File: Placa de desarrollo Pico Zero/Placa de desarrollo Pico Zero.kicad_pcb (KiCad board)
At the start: 2 copper layers, 91.5 x 101.6 mm, 33 parts, among them J1 LEFT-MALE, J2 RIGHT-MALE, J3 DOWN-MALE, J4 DOWN-FEMALE, J5 LEFT-FEMALE, J6 RIGHT-FEMALE, J7 USB_A, U1 RP2040

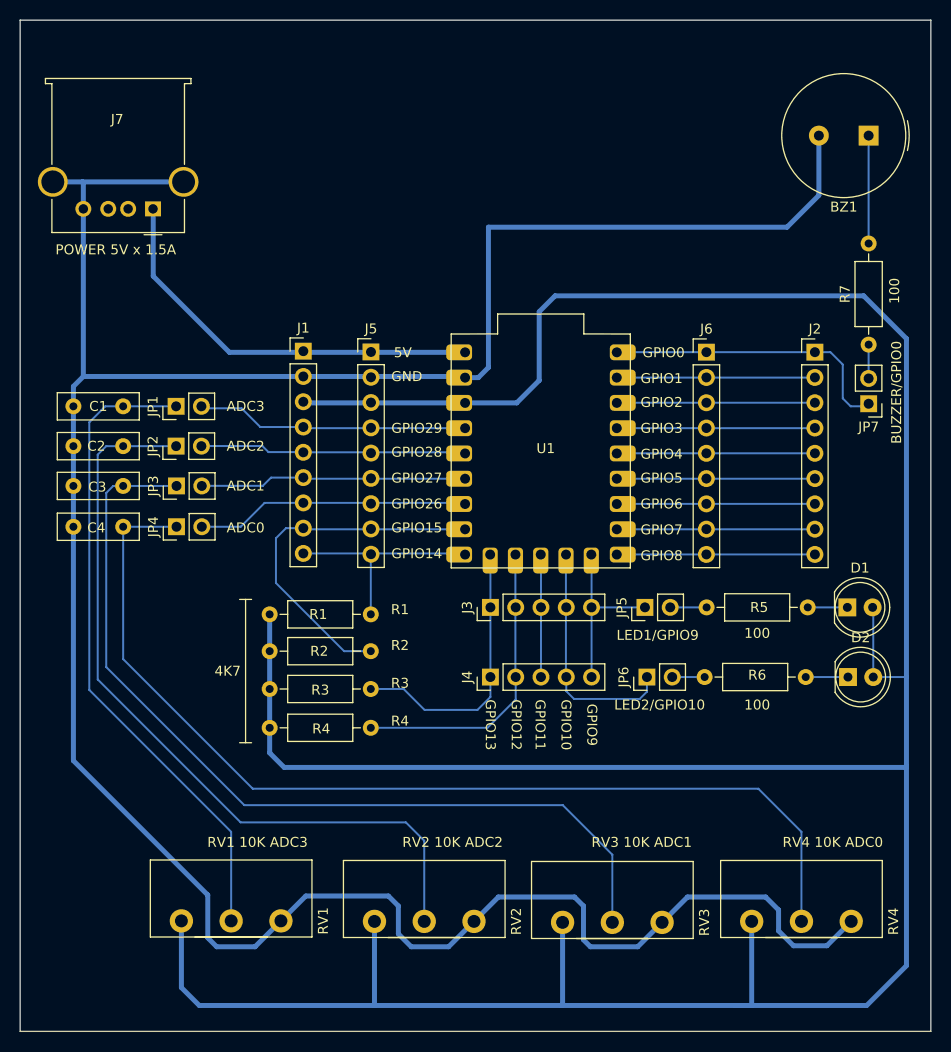
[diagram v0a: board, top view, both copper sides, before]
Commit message: Version 1.0 de la placa de desarrollor para la Pico Zero
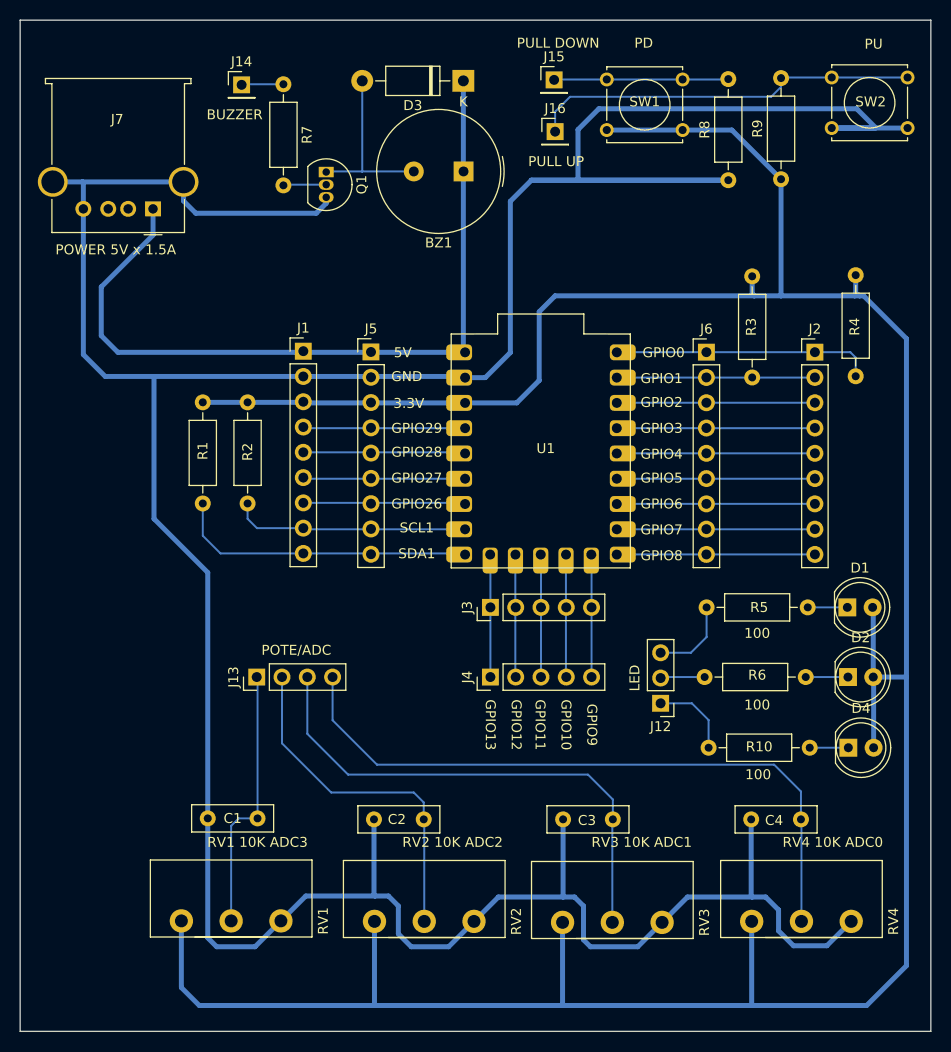
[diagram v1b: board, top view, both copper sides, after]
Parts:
- removed JP1, JP2, JP3, JP4, JP5, JP6, JP7: Jumper_2_Bridged, Connector_PinHeader_2.54mm:PinHeader_1x02_P2.54mm_Vertical
- added D3: 1N4007, Diode_THT:D_DO-41_SOD81_P10.16mm_Horizontal, F.Cu at (142.1, 22.7)
- added D4: LED, LED_THT:LED_D5.0mm, F.Cu at (180.8, 89.7)
- added J12: Conn_01x03, Connector_PinHeader_2.54mm:PinHeader_1x03_P2.54mm_Vertical, F.Cu at (161.9, 85.2)
- added J13: Conn_01x04, Connector_PinHeader_2.54mm:PinHeader_1x04_P2.54mm_Vertical, F.Cu at (121.3, 82.6)
- added J14: Conn_01x01, Connector_PinHeader_2.54mm:PinHeader_1x01_P2.54mm_Vertical, F.Cu at (119.8, 23.1)
- added J15: Conn_01x01, Connector_PinHeader_2.54mm:PinHeader_1x01_P2.54mm_Vertical, F.Cu at (151.2, 22.6)
- added J16: Conn_01x01, Connector_PinHeader_2.54mm:PinHeader_1x01_P2.54mm_Vertical, F.Cu at (151.3, 27.8)
- added Q1: BC547, Package_TO_SOT_THT:TO-92_Inline, F.Cu at (128.3, 31.9)
- added R10: 100, Resistor_THT:R_Axial_DIN0207_L6.3mm_D2.5mm_P10.16mm_Horizontal, F.Cu at (166.7, 89.7)
- added R8: 10k, Resistor_THT:R_Axial_DIN0207_L6.3mm_D2.5mm_P10.16mm_Horizontal, F.Cu at (168.7, 32.7)
- added R9: 10k, Resistor_THT:R_Axial_DIN0207_L6.3mm_D2.5mm_P10.16mm_Horizontal, F.Cu at (174.0, 32.6)
- added SW1: SW_Push, Button_Switch_THT:SW_Tactile_Straight_KSL0Axx1LFTR, F.Cu at (156.5, 22.6)
- added SW2: SW_Push, Button_Switch_THT:SW_Tactile_Straight_KSL0Axx1LFTR, F.Cu at (179.1, 22.4)
- R7: value 100 -> 1k
- moved C4 74.2 mm to (176.0, 96.9)
- moved R7 64.4 mm to (124.0, 23.0), turned to -90 degrees
- moved R4 60.2 mm to (181.5, 52.4), turned to 90 degrees
- moved C3 59.5 mm to (157.1, 96.9)
- moved R3 49.5 mm to (171.1, 52.5), turned to 90 degrees
- moved C2 48.1 mm to (138.1, 96.9)
- moved C1 43.5 mm to (121.4, 96.8)
- moved BZ1 40.9 mm to (142.1, 31.8)
- moved R1 20.2 mm to (115.9, 65.2), turned to 90 degrees
- moved R2 19.3 mm to (120.4, 65.2), turned to 90 degrees
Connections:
- net 3V3_Pico renamed 3V3
- net GPIO14/SDA1 renamed SDA1
- net GPIO15/SCL1 renamed SCL1
- net Net-(JP1-A) renamed ADC0
- net Net-(JP2-A) renamed ADC1
- net Net-(JP3-A) renamed ADC3
- net Net-(JP4-A) renamed ADC4
- BZ1 pad 1: Net-(BZ1-+) -> 5V
- BZ1 pad 2: GND -> Net-(BZ1--)
- J3 pad 1: GPIO13/SCL0 -> SCL0
- J3 pad 2: GPIO12/SDA0 -> SDA0
- J4 pad 1: GPIO13/SCL0 -> SCL0
- J4 pad 2: GPIO12/SDA0 -> SDA0
- R3 pad 1: GPIO13/SCL0 -> GPIO1
- R4 pad 1: GPIO12/SDA0 -> GPIO0
- R7 pad 2: Net-(BZ1-+) -> Net-(Q1-B)
- U1 pad 16: GPIO12/SDA0 -> SDA0
- U1 pad 17: GPIO13/SCL0 -> SCL0
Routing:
- net GND: track 274.3 -> 365.1 mm
- net 5V: track 41.5 -> 88.8 mm
- net ADC1: track 78.4 -> 35.3 mm
- net Net-(J16-Pin_1): track 0.00 -> 39.4 mm
- net ADC3: track 90.3 -> 51.5 mm
- net ADC0: track 65.4 -> 26.7 mm
- net ADC4: track 103.0 -> 67.4 mm
- net GPIO12/SDA0: track 30.3 -> 0.00 mm
- net GPIO13/SCL0: track 27.7 -> 0.00 mm
- net 3V3: track 331.7 -> 306.2 mm
- net Net-(BZ1--): track 0.00 -> 17.9 mm
- net Net-(J15-Pin_1): track 0.00 -> 17.5 mm
- net SCL1: track 36.3 -> 23.8 mm
- net SCL0: track 0.00 -> 12.3 mm
- net SDA0: track 0.00 -> 12.3 mm
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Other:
- board text added: "3.3V"
- board text added: "BUZZER"
- board text added: "LED"
- board text added: "PD"
- board text added: "POTE/ADC"
- board text added: "PU"
- board text added: "PULL DOWN"
- board text added: "PULL UP"
- board text added: "SCL1"
- board text added: "SDA1"
- board text removed: "4K7"
- board text removed: "ADC0"
- board text removed: "ADC1"
- board text removed: "ADC2"
- board text removed: "ADC3"
- board text removed: "BUZZER/GPIO0"
- board text removed: "GPIO14"
- board text removed: "GPIO15"
- board text removed: "LED1/GPIO9"
- board text removed: "LED2/GPIO10"
- board text removed: "R1"
- board text removed: "R2"
- board text removed: "R3"
- board text removed: "R4"
